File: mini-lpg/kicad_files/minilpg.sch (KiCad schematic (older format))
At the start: 20 parts, among them J1 CV, J2 IN, J3 OUT, SW1 LP/BP, SW2 LPG/VCA, SW3 MINIDIST, U1 NSL-32

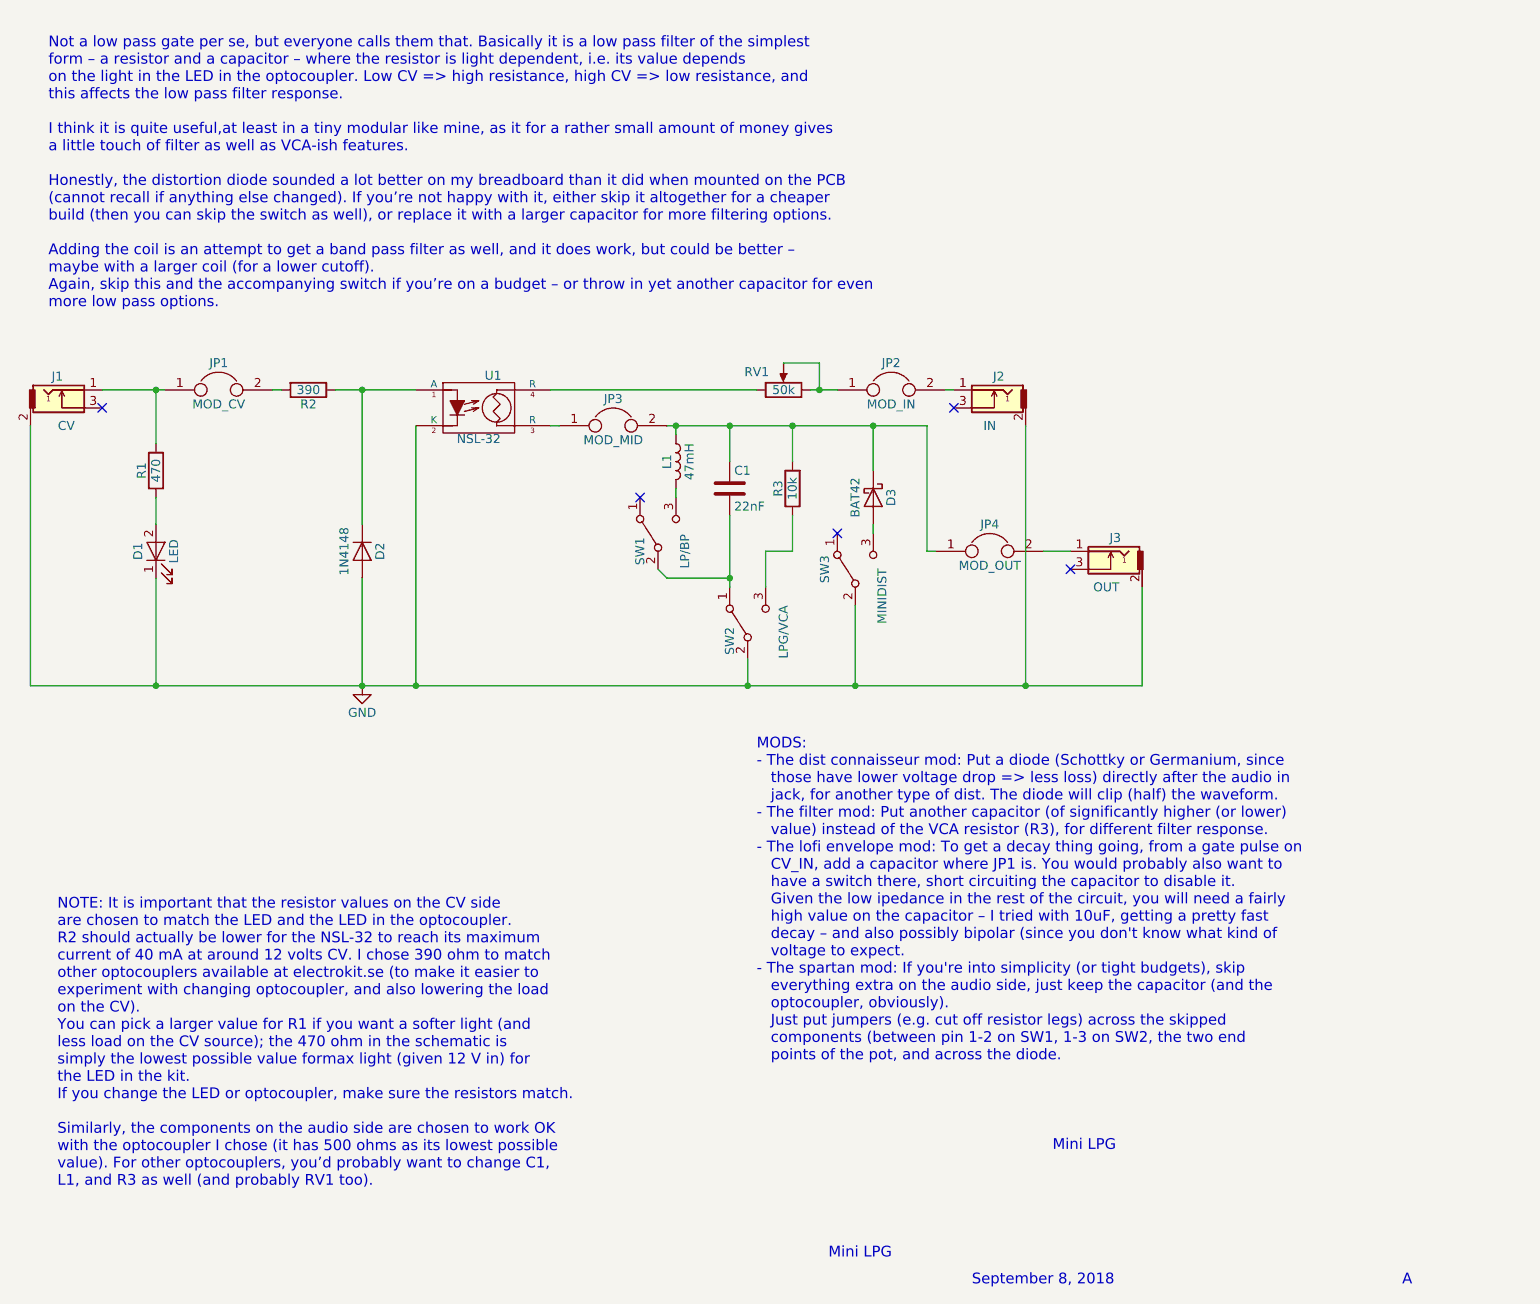
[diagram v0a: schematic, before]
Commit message: Brush up docs on ringmod and mini-LPG
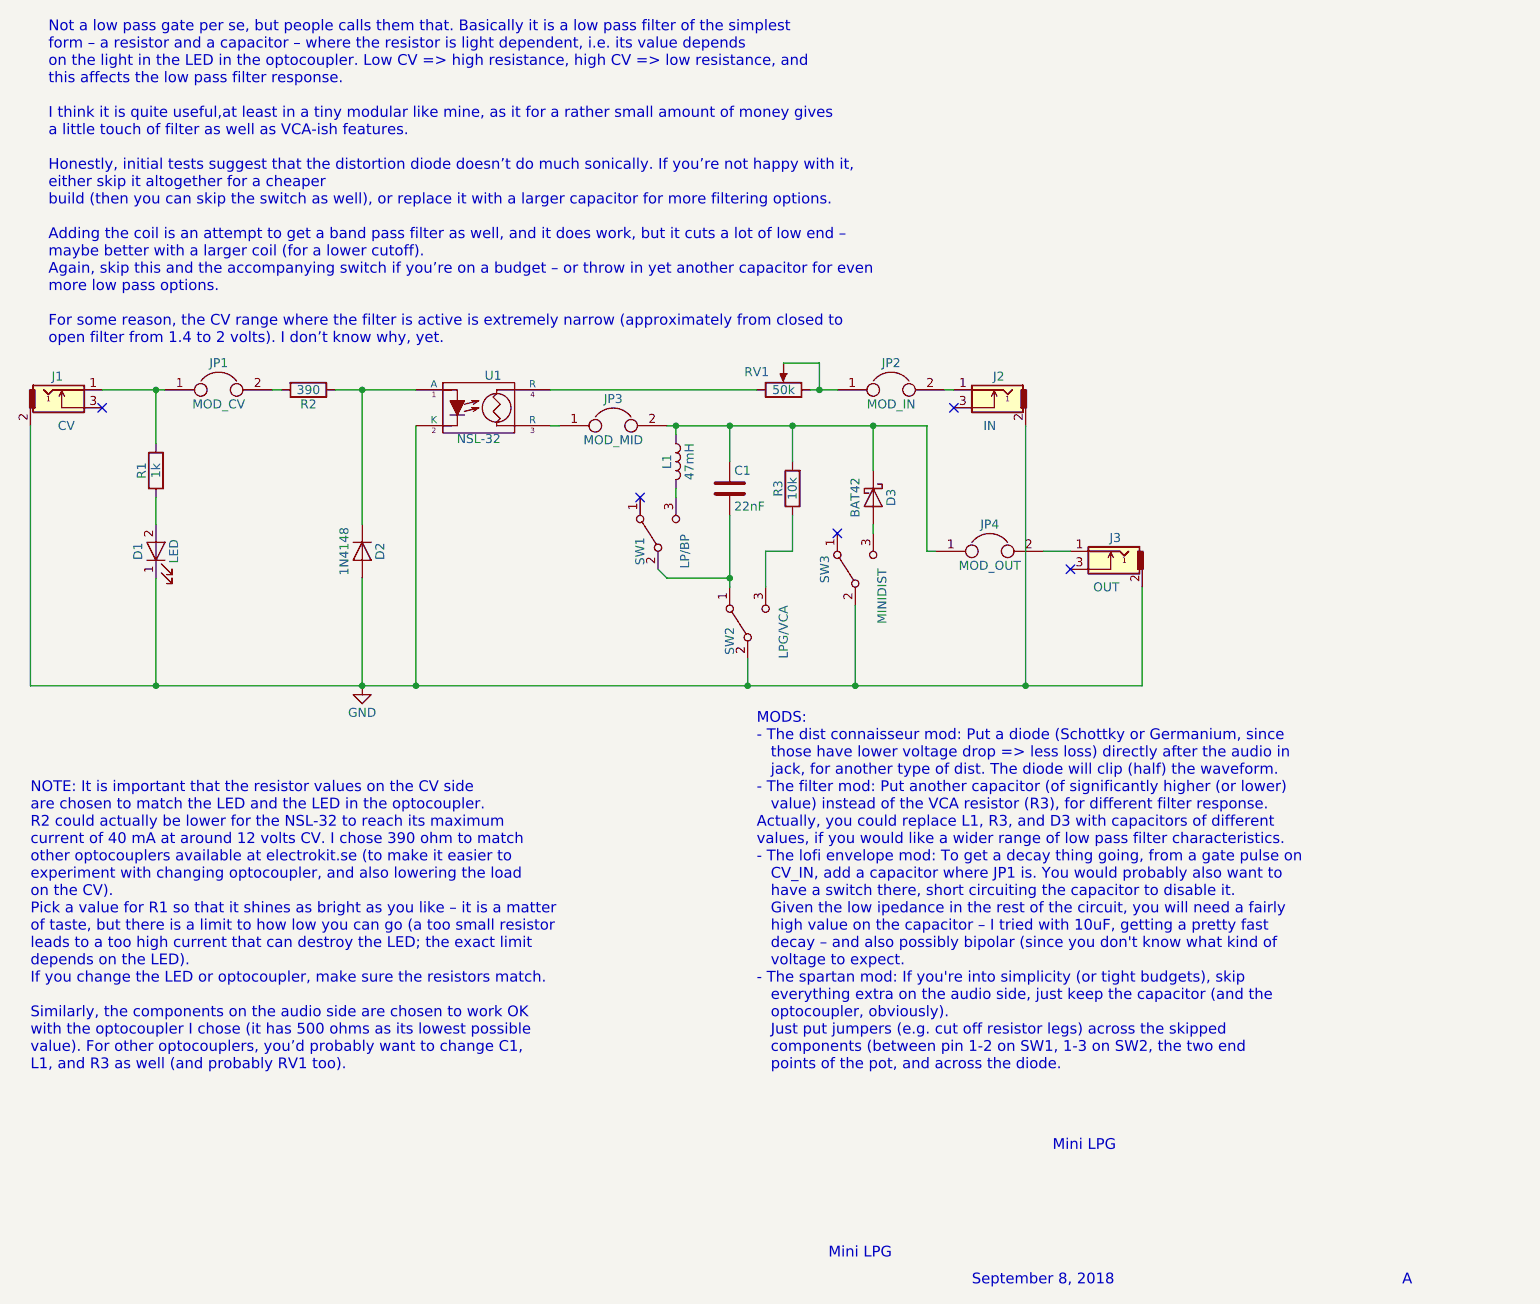
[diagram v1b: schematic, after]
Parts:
- R1: value 470 -> 1k
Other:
- note added: "MODS:\n- The dist connaisseur mod: Put a diode (Schottky or Germanium, since \n those have lower voltage drop => less loss) directly after the audio in \n jack, for another type of dist. The diode will clip (half) the waveform. \n- The filter mod: Put another capacitor (of significantly higher (or lower) \n value) instead of the VCA resistor (R3), for different filter response.\nActually, you cou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"
- note added: "NOTE: It is important that the resistor values on the CV side \nare chosen to match the LED and the LED in the optocoupler.\nR2 could actually be lower for the NSL-32 to reach its maximum \ncurrent of 40 mA at around 12 volts CV. I chose 390 ohm to match \nother optocouplers available at electrokit.se (to make it easier to \nexperiment with changing optocoupler, and also lowering the load\non the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"
- note added: "Not a low pass gate per se, but people calls them that. Basically it is a low pass filter of the simplest\nform – a resistor and a capacitor – where the resistor is light dependent, i.e. its value depends \non the light in the LED in the optocoupler. Low CV => high resistance, high CV => low resistance, and \nthis affects the low pass filter response. \n\nI think it is quite useful,at least in a 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"
- note removed: "MODS:\n- The dist connaisseur mod: Put a diode (Schottky or Germanium, since \n those have lower voltage drop => less loss) directly after the audio in \n jack, for another type of dist. The diode will clip (half) the waveform. \n- The filter mod: Put another capacitor (of significantly higher (or lower) \n value) instead of the VCA resistor (R3), for different filter response. \n- The lofi envel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"
- note removed: "NOTE: It is important that the resistor values on the CV side \nare chosen to match the LED and the LED in the optocoupler.\nR2 should actually be lower for the NSL-32 to reach its maximum \ncurrent of 40 mA at around 12 volts CV. I chose 390 ohm to match \nother optocouplers available at electrokit.se (to make it easier to \nexperiment with changing optocoupler, and also lowering the load\non th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"
- note removed: "Not a low pass gate per se, but everyone calls them that. Basically it is a low pass filter of the simplest\nform – a resistor and a capacitor – where the resistor is light dependent, i.e. its value depends \non the light in the LED in the optocoupler. Low CV => high resistance, high CV => low resistance, and \nthis affects the low pass filter response. \n\nI think it is quite useful,at least in 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"
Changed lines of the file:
@@
 P 3650 3100
 F 0 "R1" V 3730 3100 50  0000 C CNN
-F 1 "470" V 3650 3100 50  0000 C CNN
+F 1 "1k" V 3650 3100 50  0000 C CNN
 F 2 "Resistors_THT:R_Axial_DIN0207_L6.3mm_D2.5mm_P7.62mm_Horizontal" V 3580 3100 50  0001 C CNN
 F 3 "" H 3650 3100 50  0001 C CNN
@@
 	-1   0    0    1
 $EndComp
-Text Notes 3100 7100 0    60   ~ 0
-NOTE: It is important that the resistor values on the CV side \nare chosen to match the LED and the LED in the optocoupler.\nR2 should actually be lower for the NSL-32 to reach its maximum \ncurrent of 40 mA at around 12 volts CV. I chose 390 ohm to match \nother optocouplers available at electrokit.se (to make it easier to \nexperiment with changing optocoupler, and also lowering the load\non the CV).\nYou can pick a larger value for R1 if you want a softer light (and \nless load on the CV source); the 470 ohm in the schematic is \nsimply the lowest possible value formax light (given 12 V in) for\nthe LED in the kit.\nIf you change the LED or optocoupler, make sure the resistors match.\n\nSimilarly, the components on the audio side are chosen to work OK\nwith the optocoupler I chose (it has 500 ohms as its lowest possible \nvalue). For other optocouplers, you’d probably want to change C1, \nL1, and R3 as well (and probably RV1 too).\n
+Text Notes 2950 6450 0    60   ~ 0
+NOTE: It is important that the resistor values on the CV side \nare chosen to match the LED and the LED in the optocoupler.\nR2 could actually be lower for the NSL-32 to reach its maximum \ncurrent of 40 mA at around 12 volts CV. I chose 390 ohm to match \nother optocouplers available at electrokit.se (to make it easier to \nexperiment with changing optocoupler, and also lowering the load\non the CV).\nPick a value for R1 so that it shines as bright as you like – it is a matter\nof taste, but there is a limit to how low you can go (a too small resistor\nleads to a too high current that can destroy the LED; the exact limit \ndepends on the LED).\nIf you change the LED or optocoupler, make sure the resistors match.\n\nSimilarly, the components on the audio side are chosen to work OK\nwith the optocoupler I chose (it has 500 ohms as its lowest possible \nvalue). For other optocouplers, you’d probably want to change C1, \nL1, and R3 as well (and probably RV1 too).\n
 $Comp
 L minilpg-rescue:SW_SPDT SW2
@@
 	0    1    1    0
 $EndComp
-Text Notes 7000 6400 0    60   ~ 0
-MODS:\n- The dist connaisseur mod: Put a diode (Schottky or Germanium, since \n   those have lower voltage drop => less loss) directly after the audio in \n   jack, for another type of dist. The diode will clip (half) the waveform. \n- The filter mod: Put another capacitor (of significantly higher (or lower) \n   value) instead of the VCA resistor (R3), for different filter response. \n- The lofi envelope mod: To get a decay thing going, from a gate pulse on\n   CV_IN, add a capacitor where JP1 is. You would probably also want to \n   have a switch there, short circuiting the capacitor to disable it. \n   Given the low ipedance in the rest of the circuit, you will need a fairly \n   high value on the capacitor – I tried with 10uF, getting a pretty fast \n   decay – and also possibly bipolar (since you don't know what kind of \n   voltage to expect.\n- The spartan mod: If you're into simplicity (or tight budgets), skip \n   everything extra on the audio side, just keep the capacitor (and the \n   optocoupler, obviously). \n   Just put jumpers (e.g. cut off resistor legs) across the skipped \n   components (between pin 1-2 on SW1, 1-3 on SW2, the two end \n   points of the pot, and across the diode.
+Text Notes 7000 6450 0    60   ~ 0
+MODS:\n- The dist connaisseur mod: Put a diode (Schottky or Germanium, since \n   those have lower voltage drop => less loss) directly after the audio in \n   jack, for another type of dist. The diode will clip (half) the waveform. \n- The filter mod: Put another capacitor (of significantly higher (or lower) \n   value) instead of the VCA resistor (R3), for different filter response.\nActually, you could replace L1, R3, and D3 with capacitors of different\nvalues, if you would like a wider range of low pass filter characteristics. \n- The lofi envelope mod: To get a decay thing going, from a gate pulse on\n   CV_IN, add a capacitor where JP1 is. You would probably also want to \n   have a switch there, short circuiting the capacitor to disable it. \n   Given the low ipedance in the rest of the circuit, you will need a fairly \n   high value on the capacitor – I tried with 10uF, getting a pretty fast \n   decay – and also possibly bipolar (since you don't know what kind of \n   voltage to expect.\n- The spartan mod: If you're into simplicity (or tight budgets), skip \n   everything extra on the audio side, just keep the capacitor (and the \n   optocoupler, obviously). \n   Just put jumpers (e.g. cut off resistor legs) across the skipped \n   components (between pin 1-2 on SW1, 1-3 on SW2, the two end \n   points of the pot, and across the diode.
 $Comp
 L minilpg-rescue:SW_SPDT SW1
@@
 Wire Wire Line
 	7950 3550 8000 3550
-Text Notes 3050 2200 0    60   ~ 0
-Not a low pass gate per se, but everyone calls them that. Basically it is a low pass filter of the simplest\nform – a resistor and a capacitor – where the resistor is light dependent, i.e. its value depends \non the light in the LED in the optocoupler. Low CV => high resistance, high CV => low resistance, and \nthis affects the low pass filter response. \n\nI think it is quite useful,at least in a tiny modular like mine, as it for a rather small amount of money gives \na little touch of filter as well as VCA-ish features. \n\nHonestly, the distortion diode sounded a lot better on my breadboard than it did when mounted on the PCB \n(cannot recall if anything else changed). If you’re not happy with it, either skip it altogether for a cheaper \nbuild (then you can skip the switch as well), or replace it with a larger capacitor for more filtering options.\n\nAdding the coil is an attempt to get a band pass filter as well, and it does work, but could be better – \nmaybe with a larger coil (for a lower cutoff). \nAgain, skip this and the accompanying switch if you’re on a budget – or throw in yet another capacitor for even \nmore low pass options.
+Text Notes 3050 2400 0    60   ~ 0
+Not a low pass gate per se, but people calls them that. Basically it is a low pass filter of the simplest\nform – a resistor and a capacitor – where the resistor is light dependent, i.e. its value depends \non the light in the LED in the optocoupler. Low CV => high resistance, high CV => low resistance, and \nthis affects the low pass filter response. \n\nI think it is quite useful,at least in a tiny modular like mine, as it for a rather small amount of money gives \na little touch of filter as well as VCA-ish features. \n\nHonestly, initial tests suggest that the distortion diode doesn’t do much sonically. If you’re not happy with it, \neither skip it altogether for a cheaper \nbuild (then you can skip the switch as well), or replace it with a larger capacitor for more filtering options.\n\nAdding the coil is an attempt to get a band pass filter as well, and it does work, but it cuts a lot of low end – \nmaybe better with a larger coil (for a lower cutoff). \nAgain, skip this and the accompanying switch if you’re on a budget – or throw in yet another capacitor for even \nmore low pass options.\n\nFor some reason, the CV range where the filter is active is extremely narrow (approximately from closed to \nopen filter from 1.4 to 2 volts). I don’t know why, yet.
 Text Notes 7400 7500 0    60   ~ 0
 Mini LPG\n
